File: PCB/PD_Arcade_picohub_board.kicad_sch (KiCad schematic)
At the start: 33 parts, among them J1 Partition_Lights_L, J10 Circle_LED, J11 Cross_LED, J12 Square_LED, J13 Triangle_LED, J14 Slider LEDs 5V power, J15 5V_In, J2 Start_button, J3 12V_In, J4 Circle_button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

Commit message: PCB readme
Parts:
- renumbered U3 to U1, U6 to U3, U1 to U4

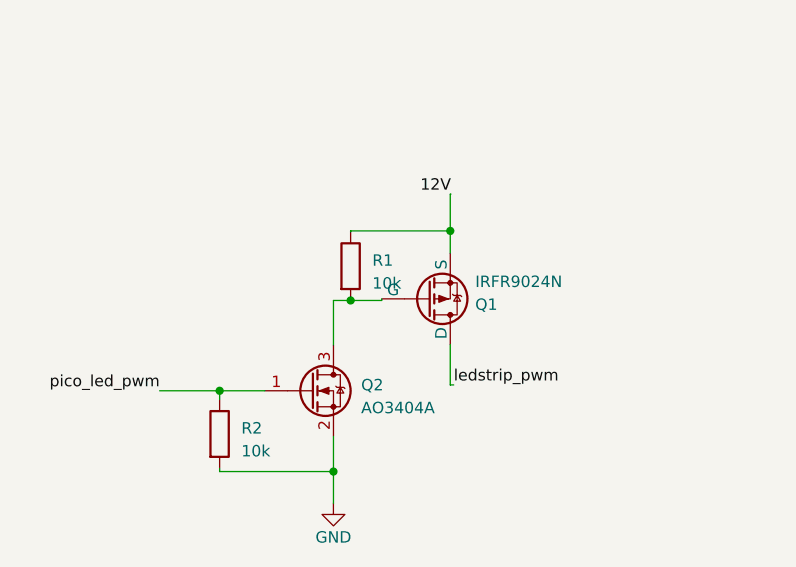
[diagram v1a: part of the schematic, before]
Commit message: R1 fix to 1k
10k do not work
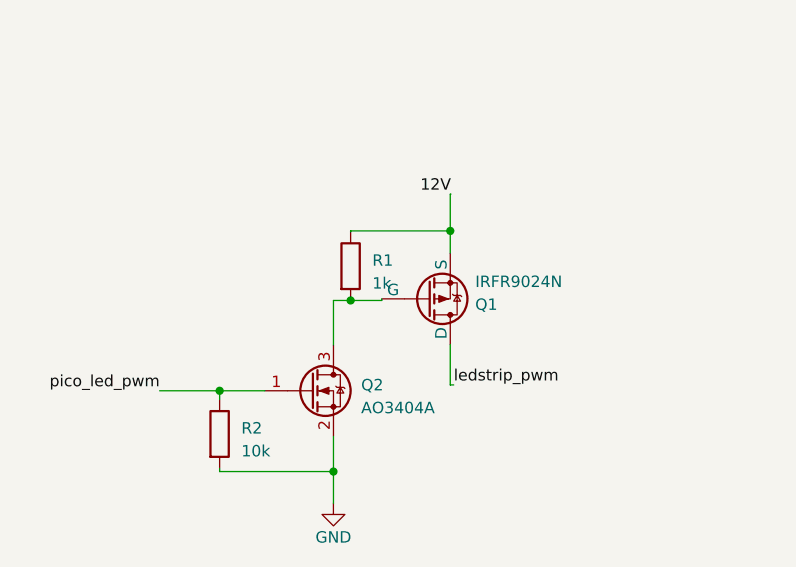
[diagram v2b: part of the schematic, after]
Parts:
- R1: value 10k -> 1k
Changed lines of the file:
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@@
       (effects (font (size 1.27 1.27)) (justify left))
     )
-    (property "Value" "10k" (at 49.53 129.1336 0)
+    (property "Value" "1k" (at 49.53 129.1336 0)
       (effects (font (size 1.27 1.27)) (justify left))
     )
